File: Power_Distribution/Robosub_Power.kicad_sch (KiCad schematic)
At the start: 47 parts, among them J1 1135333, J10 1135333, J14 Conn_01x04, J2 1135333, J3 1135333, J4 1135333, J5 1135333, J6 1135333, J7 1135333, J8 1135333, J9 1135333, U1 INA300AIDSQT, U2 SN74LVC1G97DBVR, U3 AUIR3241STR, U4 BSC0702LSATMA1, U5 BSC0702LSATMA1, U6 BSC0702LSATMA1, U7 NVTR01P02LT1G, U8 NVTR01P02LT1G

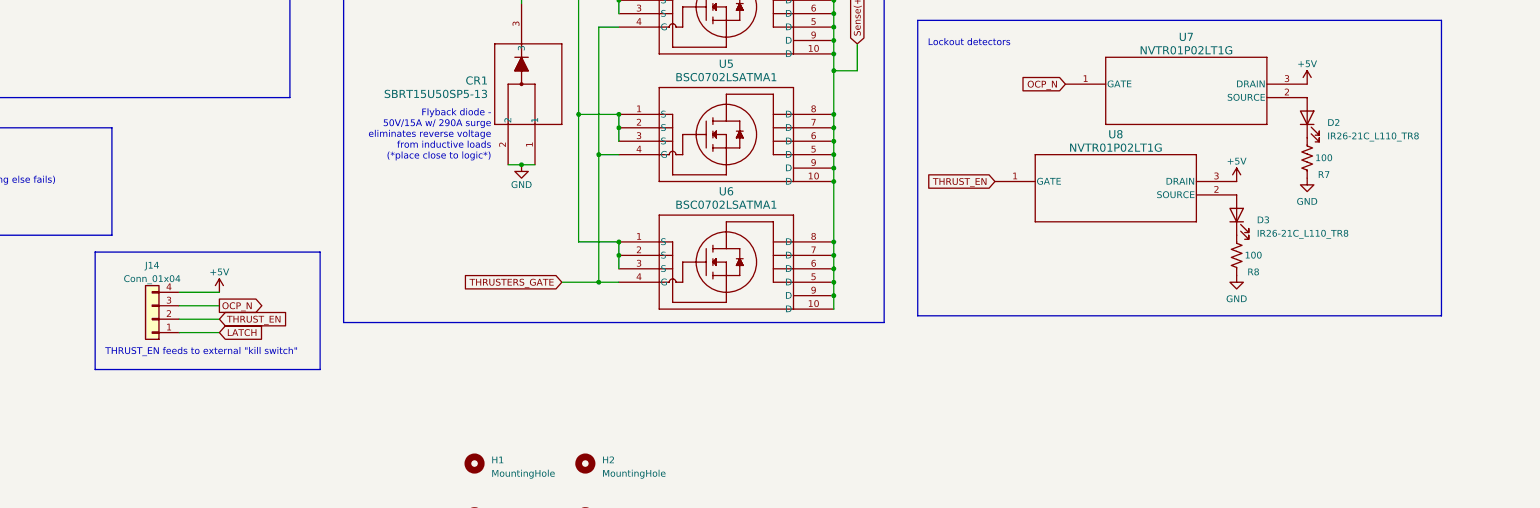
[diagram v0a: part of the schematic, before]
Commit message: power rev2[fix diodes, ground loop, silkscreen]
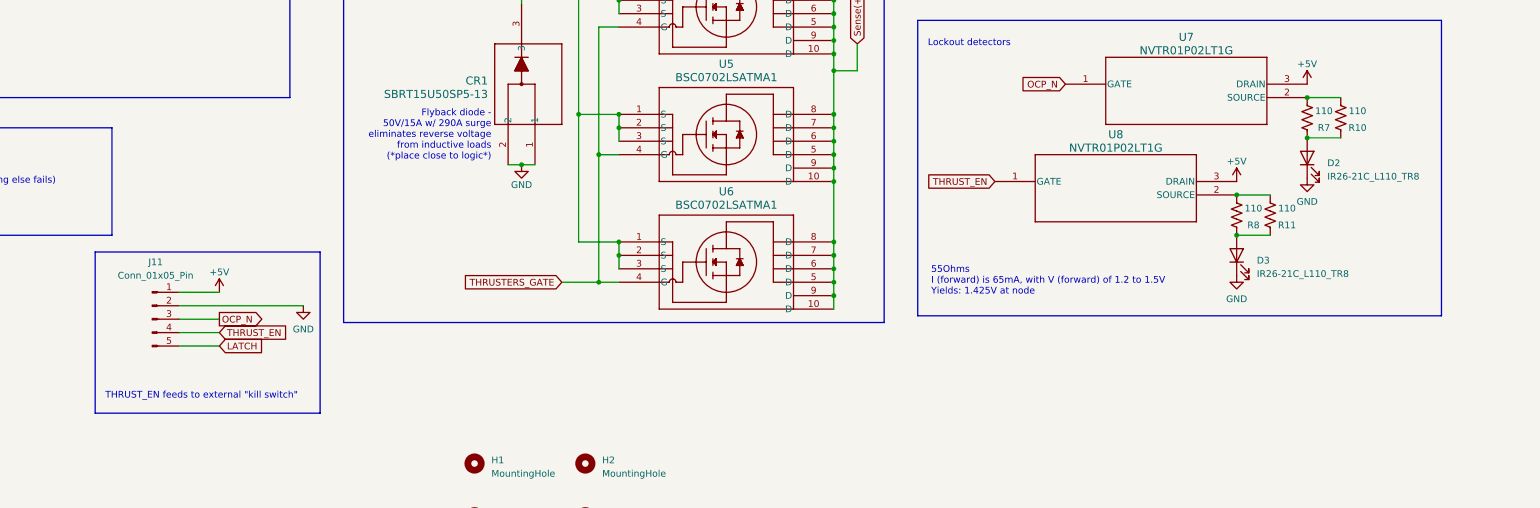
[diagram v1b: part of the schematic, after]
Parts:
- removed J14: Conn_01x04, Connector_PinHeader_2.54mm:PinHeader_1x04_P2.54mm_Vertical, symbol Connector_Generic:Conn_01x04
- added J11: Conn_01x05_Pin, Connector_PinHeader_2.54mm:PinHeader_1x05_P2.54mm_Vertical, symbol Connector:Conn_01x05_Pin
- added R10, R11: 110, Resistor_SMD:R_0805_2012Metric_Pad1.20x1.40mm_HandSolder, symbol Device:R_US
- R7, R8: value 100 -> 110; MFR YAGEO -> Susumu; MFR S/N RC0805FR-07100RL -> RG2012N-111-W-T1; Supplier 1 https://www.digikey.com/en/products/detail/yageo/RC0805FR-0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 -> https://www.digikey.com/en/products/detail/susumu/RG2012N-1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; Supplier 1 S/N 311-100CRCT-ND -> 408-RG2012N-111-W-T1CT-ND
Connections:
- net +5V: now also J11.1 (Pin_1)
- net GND: now also D2.1 (K), D3.1 (K), J11.2 (Pin_2); no longer R7.1, R8.1
- net LATCH: now also J11.5 (Pin_5)
- net OCP_N: now also J11.3 (Pin_3)
- net THRUST_EN: now also J11.4 (Pin_4)
- net at R8.2: now also U8.2 (SOURCE), R11.2; no longer D3.1 (K)
- net at D3.2 (A): now also R8.1, R11.1; no longer U8.2 (SOURCE)
- net at D2.2 (A): now also R7.1, R10.1; no longer U7.2 (SOURCE)
- net at R7.2: now also U7.2 (SOURCE), R10.2; no longer D2.1 (K)
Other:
- note added: "55Ohms I (forward) is 65mA, with V (forward) of 1.2 to 1.5V Yields: 1.425V at node"
- company: blame- steven.clark@stanford.edu -> blame- valex@stanford.edu
- title: Test sheet -> Main
- moved on the sheet: D2, D3, R7
